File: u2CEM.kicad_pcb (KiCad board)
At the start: 6 copper layers, 188 x 66.8 mm, 24 parts, among them J1 PCIE_x4_PCIE-064-02-S-D-RA, J2 PSAS4M2130021TR

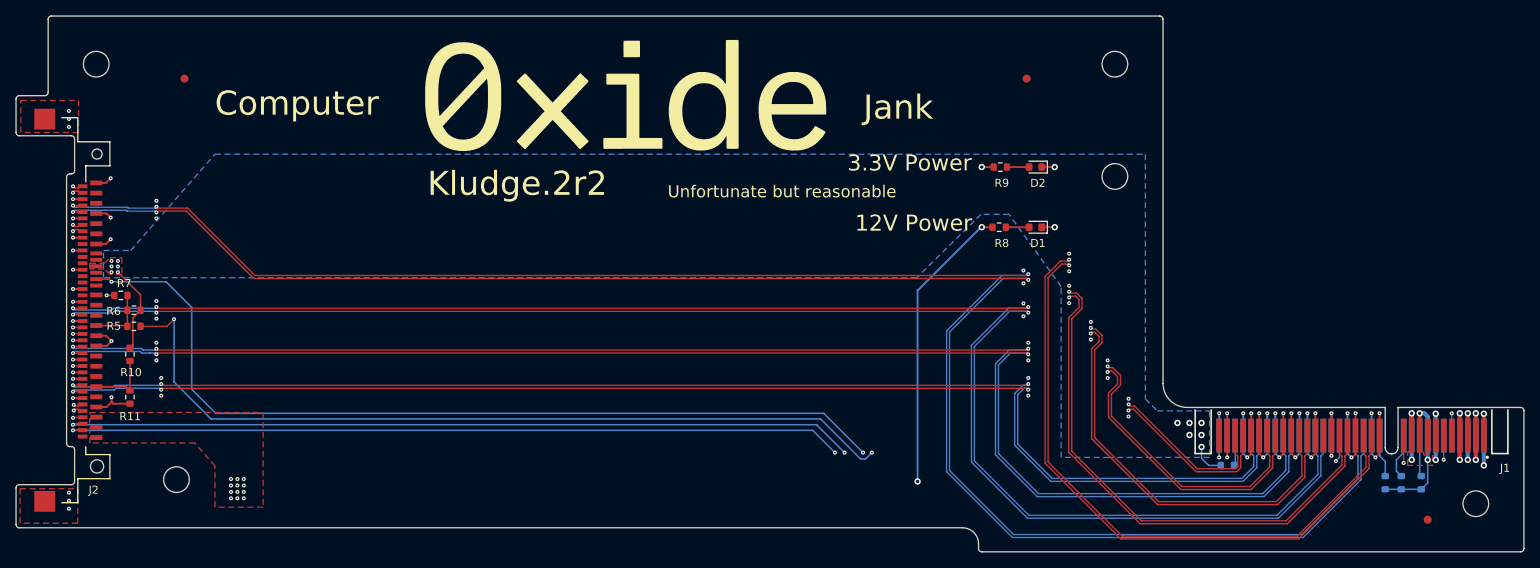
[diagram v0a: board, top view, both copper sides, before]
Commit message: initial quote request to Sierra
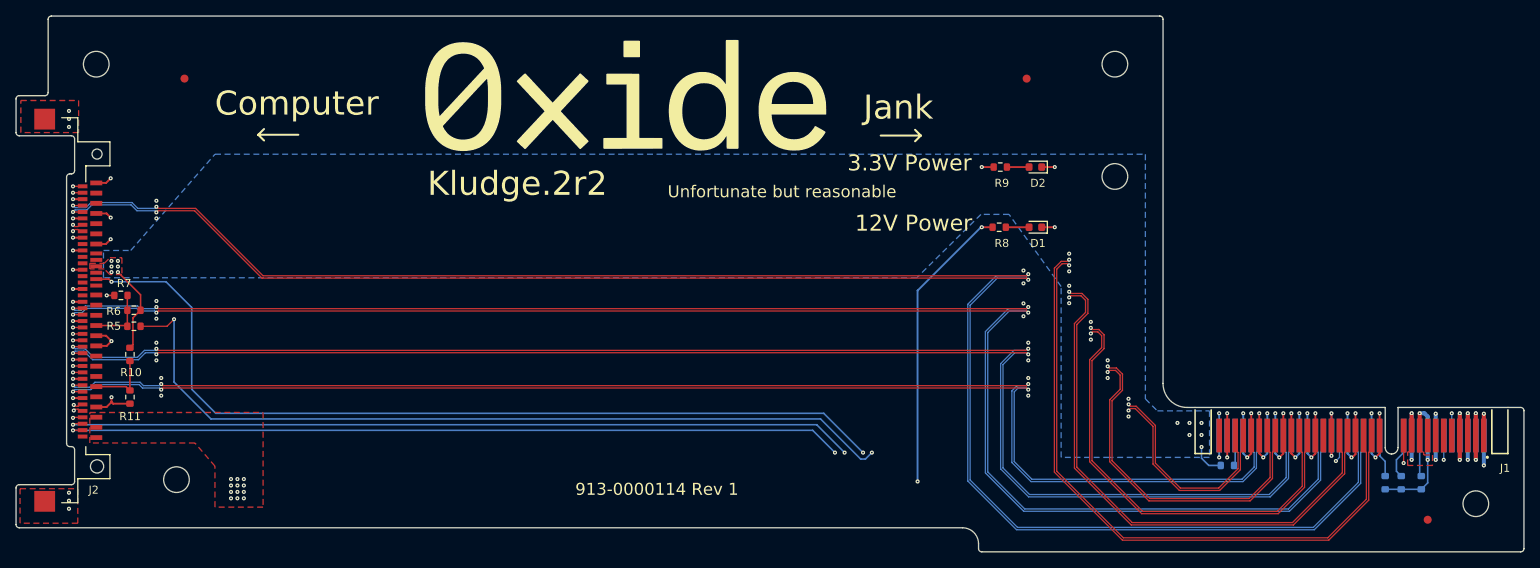
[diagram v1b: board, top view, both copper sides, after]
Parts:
- J1: value PCIE_x4_PCIE-064-02-S-D-RA -> PCIE-064-02-F-D-EMS2-BG
- R8: value 5k -> 5.11k
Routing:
- net /PER2_N: track 166.4 -> 172.1 mm
- net /PER2_P: track 167.1 -> 172.6 mm
- net /PER3_N: track 154.5 -> 159.2 mm
- net /PER3_P: track 155.1 -> 159.6 mm
- net /PER1_N: track 178.9 -> 183.2 mm
- net /PER1_P: track 179.5 -> 183.7 mm
- net /PET3_N: track 164.4 -> 167.4 mm
- net /PET0_P: track 218.5 -> 215.8 mm
- net /PET3_P: track 166.2 -> 168.8 mm
- net /PET0_N: track 216.6 -> 214.4 mm
- net /PER0_N: track 194.7 -> 196.7 mm
- net /PER0_P: track 195.3 -> 197.2 mm
- net /PET1_P: track 198.1 -> 196.3 mm
- net /REFCLK_N: track 207.1 -> 208.7 mm
- net /PET2_N: track 179.7 -> 181.1 mm
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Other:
- board text added: "913-0000114 Rev 1"
